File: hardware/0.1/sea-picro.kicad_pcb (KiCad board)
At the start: 4 copper layers, 17.8 x 33 mm, 44 parts, among them J1 USB_C_Receptacle_USB2.0, J2 0.1" x 12, J3 0.1" x 12, SW1 BOOT, SW2 RESET, U1 AP2112K-3.3, U3 W25Q128JVSIQ, U4 RP2040, Y1 12MHz

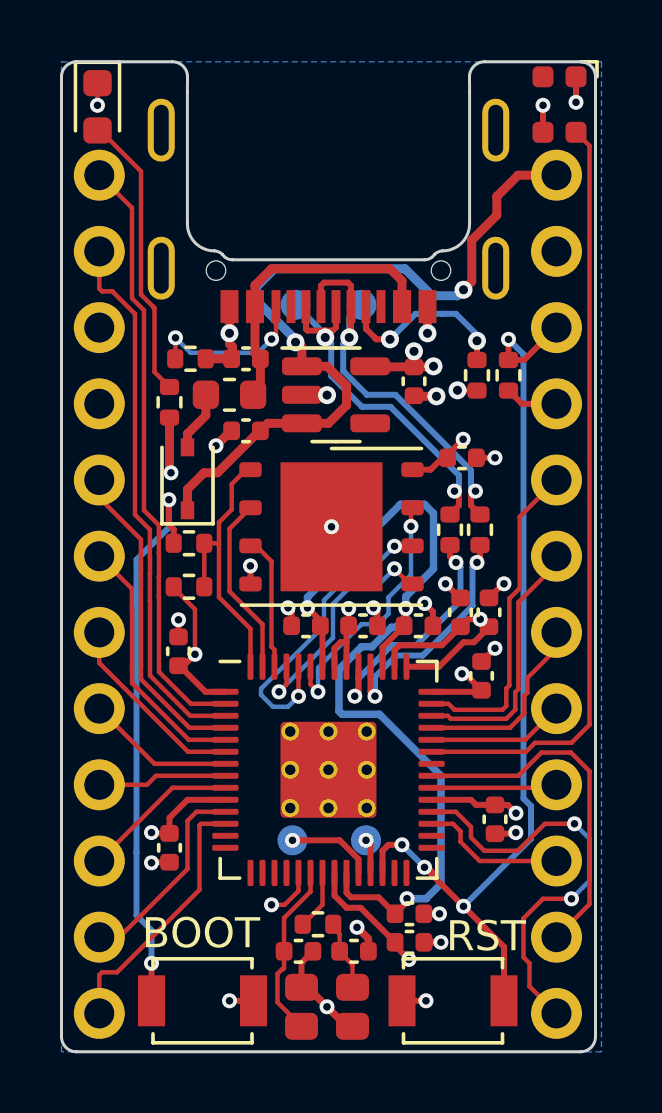
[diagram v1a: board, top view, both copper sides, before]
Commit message: clean up traces and add BOM
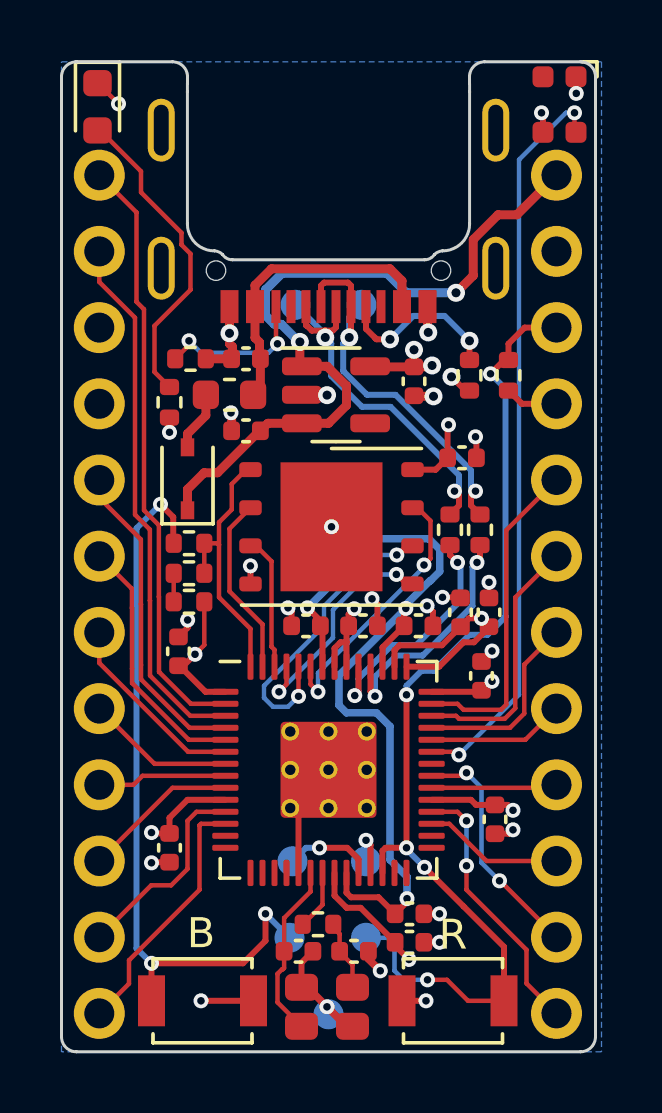
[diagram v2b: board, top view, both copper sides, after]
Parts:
- added R10: 5K1, Resistor_SMD:R_0402_1005Metric, F.Cu at (121.5, 91.8)
- added TP5: BOOT, TestPoint:TestPoint_Pad_D1.0mm, B.Cu at (124.9, 104.0)
- added TP6: GND, TestPoint:TestPoint_Pad_D1.0mm, B.Cu at (126.2, 106.5)
- added TP7: nRST, TestPoint:TestPoint_Pad_D1.0mm, B.Cu at (127.5, 104.0)
- added kibuzzard-61D6DCF8: G***, kibuzzard-61D6DCF8, B.Cu at (122.9, 92.0)
- added kibuzzard-61D6E17D: G***, kibuzzard-61D6E17D, B.Cu at (126.0, 91.8)
- D3: value WS2812B -> WS2812C-2020
- R6: value 10K -> 5K1
- U3: value W25Q128JVSIQ -> W25Q128JVPIQ
- moved LOGO1 4.25 mm to (122.0, 106.0)
- moved TP3 0.70 mm to (125.0, 101.5)
- moved TP4 0.70 mm to (127.5, 101.5)
- moved R6 0.50 mm to (121.5, 92.8), turned to 180 degrees
- moved R1 0.25 mm to (130.9, 85.2)
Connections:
- R6 pad 2: /FLASH_nCS -> Net-(R10-Pad1)
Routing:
- net Net-(R4-Pad2): track 18.9 -> 24.7 mm, vias 2 -> 3
- net /21_nCS: track 14.3 -> 8.95 mm
- net /23_MOSI: track 11.8 -> 7.94 mm, vias 0 -> 2
- net /nRST: track 31.5 -> 35.1 mm, vias 4 -> 5
- net +1V1: track 31.1 -> 27.7 mm
- net +3V3: track 38.1 -> 35.6 mm
- net GND: track 24.4 -> 25.6 mm, vias 27 -> 26
- net +5V: track 26.3 -> 25.3 mm
- net Net-(D2-Pad2): track 9.60 -> 10.6 mm
- net Net-(R10-Pad1): track 0.00 -> 0.95 mm
- net /LED_DO: track 25.6 -> 24.8 mm, vias 0 -> 2
- net /SWDIO: track 1.15 -> 1.85 mm
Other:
- board text added: "+"
- board text added: "-"
- board text added: "0"
- board text added: "1"
- board text added: "2"
- board text added: "20"
- board text added: "21"
- board text added: "22"
- board text added: "23"
- board text added: "26/A0"
- board text added: "27/A1"
- board text added: "28/A2"
- board text added: "29/A3"
- board text added: "3"
- board text added: "3V3"
- board text added: "4"
- board text added: "5"
- board text added: "6"
- board text added: "7"
- board text added: "8"
- board text added: "9"
- board text added: "B"
- board text added: "CLK"
- board text added: "G"
- board text added: "GND"
- board text added: "IO"
- board text added: "R"
- board text added: "US"
- board text added: "VB"
- board text removed: "BOOT"

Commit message: update dates and revision number
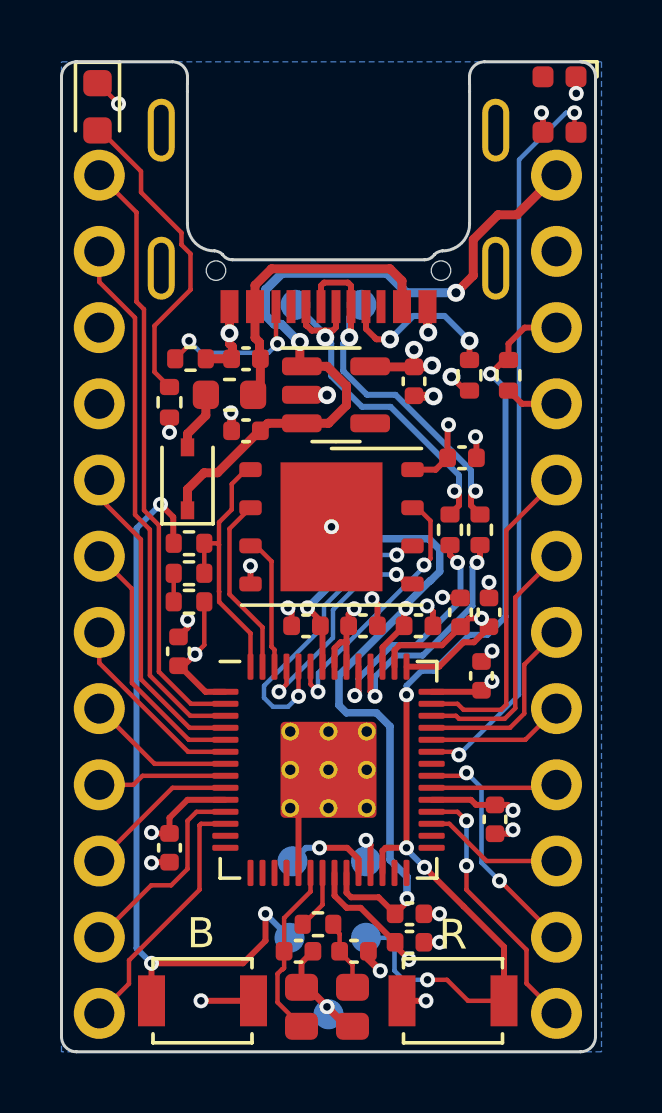
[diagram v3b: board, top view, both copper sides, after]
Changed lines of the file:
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@@
   (paper "A4")
   (title_block
-    (title "Sea Micro")
-    (date "2020-12-11")
-    (rev "0.3")
-    (company "Josh Johnson and Custom KBD")
+    (title "Sea Picro")
+    (date "2022-01-07")
+    (rev "0.1")
+    (company "Josh Johnson")
   )
   (layers
@@
   (segment (start 122.7625 97.8) (end 121.519589 97.8) (width 0.15) (layer "F.Cu") (net 22))
   (segment (start 118.56 94.840411) (end 118.56 93.82) (width 0.15) (layer "F.Cu") (net 22))
-  (segment (start 119.650499 95.031549) (end 119.650499 93.009653) (width 0.15) (layer "F.Cu") (net 23))
+  (segment (start 119.646948 95.503787) (end 119.646948 92.366948) (width 0.15) (layer "F.Cu") (net 23))
+  (segment (start 121.543161 97.4) (end 119.646948 95.503787) (width 0.15) (layer "F.Cu") (net 23))
   (segment (start 122.7625 97.4) (end 121.543161 97.4) (width 0.15) (layer "F.Cu") (net 23))
-  (segment (start 119.65097 95.507809) (end 119.65097 95.03202) (width 0.15) (layer "F.Cu") (net 23))
   (segment (start 119.646948 92.366948) (end 118.56 91.28) (width 0.15) (layer "F.Cu") (net 23))
-  (segment (start 119.650499 93.009653) (end 119.646947 93.0061) (width 0.15) (layer "F.Cu") (net 23))
-  (segment (start 121.543161 97.4) (end 119.65097 95.507809) (width 0.15) (layer "F.Cu") (net 23))
-  (segment (start 119.646947 93.0061) (end 119.646948 92.366948) (width 0.15) (layer "F.Cu") (net 23))
-  (segment (start 119.65097 95.03202) (end 119.650499 95.031549) (width 0.15) (layer "F.Cu") (net 23))
-  (segment (start 118.56 89.333572) (end 118.56 88.74) (width 0.15) (layer "F.Cu") (net 24))
-  (segment (start 121.566733 97) (end 119.95049 95.383757) (width 0.15) (layer "F.Cu") (net 24))
-  (segment (start 119.95001 92.885592) (end 119.946459 92.882041) (width 0.15) (layer "F.Cu") (net 24))
-  (segment (start 119.95049 94.907968) (end 119.95001 94.907488) (width 0.15) (layer "F.Cu") (net 24))
   (segment (start 119.946459 90.720031) (end 118.56 89.333572) (width 0.15) (layer "F.Cu") (net 24))
-  (segment (start 119.946459 92.882041) (end 119.946459 90.720031) (width 0.15) (layer "F.Cu") (net 24))
-  (segment (start 119.95001 94.907488) (end 119.95001 92.885592) (width 0.15) (layer "F.Cu") (net 24))
   (segment (start 122.7625 97) (end 121.566733 97) (width 0.15) (layer "F.Cu") (net 24))
-  (segment (start 119.95049 95.383757) (end 119.95049 94.907968) (width 0.15) (layer "F.Cu") (net 24))
+  (segment (start 119.946459 95.379726) (end 119.946459 90.720031) (width 0.15) (layer "F.Cu") (net 24))
+  (segment (start 118.56 89.333572) (end 118.56 88.74) (width 0.15) (layer "F.Cu") (net 24))
+  (segment (start 121.566733 97) (end 119.946459 95.379726) (width 0.15) (layer "F.Cu") (net 24))
+  (segment (start 120.24597 90.39202) (end 120.24597 95.255665) (width 0.15) (layer "F.Cu") (net 25))
+  (segment (start 120.24597 95.255665) (end 121.590305 96.6) (width 0.15) (layer "F.Cu") (net 25))
   (segment (start 118.56 81.12) (end 118.56 82.140411) (width 0.15) (layer "F.Cu") (net 25))
-  (segment (start 120.25049 95.260185) (end 121.590305 96.6) (width 0.15) (layer "F.Cu") (net 25))
-  (segment (start 120.24597 90.39202) (end 120.24597 92.75798) (width 0.15) (layer "F.Cu") (net 25))
-  (segment (start 120.250489 92.762499) (end 120.25049 95.260185) (width 0.15) (layer "F.Cu") (net 25))
-  (segment (start 121.590305 96.6) (end 122.7625 96.6) (width 0.15) (layer "F.Cu") (net 25))
   (segment (start 119.750489 89.896539) (end 120.24597 90.39202) (width 0.15) (layer "F.Cu") (net 25))
-  (segment (start 119.750489 83.3309) (end 119.750489 89.896539) (width 0.15) (layer "F.Cu") (net 25))
-  (segment (start 120.24597 92.75798) (end 120.250489 92.762499) (width 0.15) (layer "F.Cu") (net 25))
   (segment (start 118.56 82.140411) (end 119.750489 83.3309) (width 0.15) (layer "F.Cu") (net 25))
-  (segment (start 120.05 83.05) (end 120.05 89.75) (width 0.15) (layer "F.Cu") (net 26))
-  (segment (start 119.8 82.8) (end 120.05 83.05) (width 0.15) (layer "F.Cu") (net 26))
-  (segment (start 120.54548 90.24548) (end 120.54548 92.633918) (width 0.15) (layer "F.Cu") (net 26))
-  (segment (start 120.05 89.75) (end 120.54548 90.24548) (width 0.15) (layer "F.Cu") (net 26))
-  (segment (start 120.55 95.136123) (end 121.613877 96.2) (width 0.15) (layer "F.Cu") (net 26))
+  (segment (start 119.750489 83.3309) (end 119.750489 89.896539) (width 0.15) (layer "F.Cu") (net 25))
+  (segment (start 121.590305 96.6) (end 122.7625 96.6) (width 0.15) (layer "F.Cu") (net 25))
+  (segment (start 120.54548 95.131603) (end 121.613877 96.2) (width 0.15) (layer "F.Cu") (net 26))
   (segment (start 121.613877 96.2) (end 122.7625 96.2) (width 0.15) (layer "F.Cu") (net 26))
-  (segment (start 120.54548 92.633918) (end 120.55 92.638438) (width 0.15) (layer "F.Cu") (net 26))
-  (segment (start 119.8 79.82) (end 119.8 82.8) (width 0.15) (layer "F.Cu") (net 26))
-  (segment (start 120.55 92.638438) (end 120.55 95.136123) (width 0.15) (layer "F.Cu") (net 26))
   (segment (start 118.56 78.58) (end 119.8 79.82) (width 0.15) (layer "F.Cu") (net 26))
+  (segment (start 119.8 79.82) (end 119.8 82.8) (width 0.15) (layer "F.Cu") (net 26))
+  (segment (start 120.54548 90.24548) (end 120.54548 95.131603) (width 0.15) (layer "F.Cu") (net 26))
+  (segment (start 120.05 83.05) (end 120.05 89.75) (width 0.15) (layer "F.Cu") (net 26))
+  (segment (start 120.05 89.75) (end 120.54548 90.24548) (width 0.15) (layer "F.Cu") (net 26))
+  (segment (start 119.8 82.8) (end 120.05 83.05) (width 0.15) (layer "F.Cu") (net 26))
   (segment (start 130.5 96.2) (end 130.7 96.4) (width 0.15) (layer "F.Cu") (net 27))
   (segment (start 130.7 96.4) (end 131.95 96.4) (width 0.15) (layer "F.Cu") (net 27))
@@
   (segment (start 122.01 90.85) (end 122.5 90.85) (width 0.15) (layer "F.Cu") (net 35))
   (segment (start 123.455 88.395) (end 122.975 88.875) (width 0.15) (layer "F.Cu") (net 35))
-  (segment (start 122.55 92.65) (end 123.6 93.7) (width 0.15) (layer "F.Cu") (net 35))
-  (segment (start 123.6 93.7) (end 123.6 94.9625) (width 0.15) (layer "F.Cu") (net 35))
+  (segment (start 122.55 92.461562) (end 122.55452 92.466082) (width 0.15) (layer "F.Cu") (net 35))
+  (segment (start 123.6 93.85) (end 123.6 94.9625) (width 0.15) (layer "F.Cu") (net 35))
   (segment (start 122.5 90.85) (end 122.55 90.9) (width 0.15) (layer "F.Cu") (net 35))
   (segment (start 123.6 88.395) (end 123.455 88.395) (width 0.15) (layer "F.Cu") (net 35))
   (segment (start 122.55 90.15) (end 122.55 90.9) (width 0.15) (layer "F.Cu") (net 35))
   (segment (start 122.975 88.875) (end 122.975 89.725) (width 0.15) (layer "F.Cu") (net 35))
+  (segment (start 122.55 90.9) (end 122.55 92.461562) (width 0.15) (layer "F.Cu") (net 35))
   (segment (start 122.975 89.725) (end 122.55 90.15) (width 0.15) (layer "F.Cu") (net 35))
-  (segment (start 122.55 90.9) (end 122.55 92.65) (width 0.15) (layer "F.Cu") (net 35))
+  (segment (start 122.55452 92.466082) (end 122.55452 92.80452) (width 0.15) (layer "F.Cu") (net 35))
   (segment (start 122.06 91.85) (end 122.06 90.85) (width 0.15) (layer "F.Cu") (net 35))
+  (segment (start 122.55452 92.80452) (end 123.6 93.85) (width 0.15) (layer "F.Cu") (net 35))
   (segment (start 121.025489 90.835489) (end 121.025489 89.975489) (width 0.2) (layer "F.Cu") (net 36))
   (segment (start 123.35 104.85) (end 124.1 104.1) (width 0.2) (layer "F.Cu") (net 36))
@@
   (via (at 127.45 100.75) (size 0.5) (drill 0.25) (layers "F.Cu" "B.Cu") (net 41))
   (segment (start 127.45 100.75) (end 127.45 101.45) (width 0.2) (layer "B.Cu") (net 41))
-  (segment (start 124 94.9625) (end 124 93.55) (width 0.15) (layer "F.Cu") (net 43))
+  (segment (start 124 93.65) (end 122.9 92.55) (width 0.15) (layer "F.Cu") (net 43))
   (segment (start 122.9 90.365) (end 123.6 89.665) (width 0.15) (layer "F.Cu") (net 43))
-  (segment (start 124 93.55) (end 122.9 92.45) (width 0.15) (layer "F.Cu") (net 43))
-  (segment (start 122.9 92.45) (end 122.9 90.365) (width 0.15) (layer "F.Cu") (net 43))
+  (segment (start 124 94.9625) (end 124 93.65) (width 0.15) (layer "F.Cu") (net 43))
+  (segment (start 122.9 92.55) (end 122.9 90.365) (width 0.15) (layer "F.Cu") (net 43))
   (segment (start 124.3 91.45) (end 123.785 90.935) (width 0.15) (layer "F.Cu") (net 44))
   (segment (start 123.785 90.935) (end 123.6 90.935) (width 0.15) (layer "F.Cu") (net 44))
